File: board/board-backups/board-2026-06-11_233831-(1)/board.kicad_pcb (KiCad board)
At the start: 2 copper layers, 42.6 x 75.4 mm, 27 parts, among them J1 port attiny, J10 BMS Bat +, J11 BMS Bat gnd, J12 BMS out -, J13 BMS in +5v, J14 BMS in gnd, J15 alim mp3 -, J17 next, J18 vol -, J2 Conn_01x02_Pin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

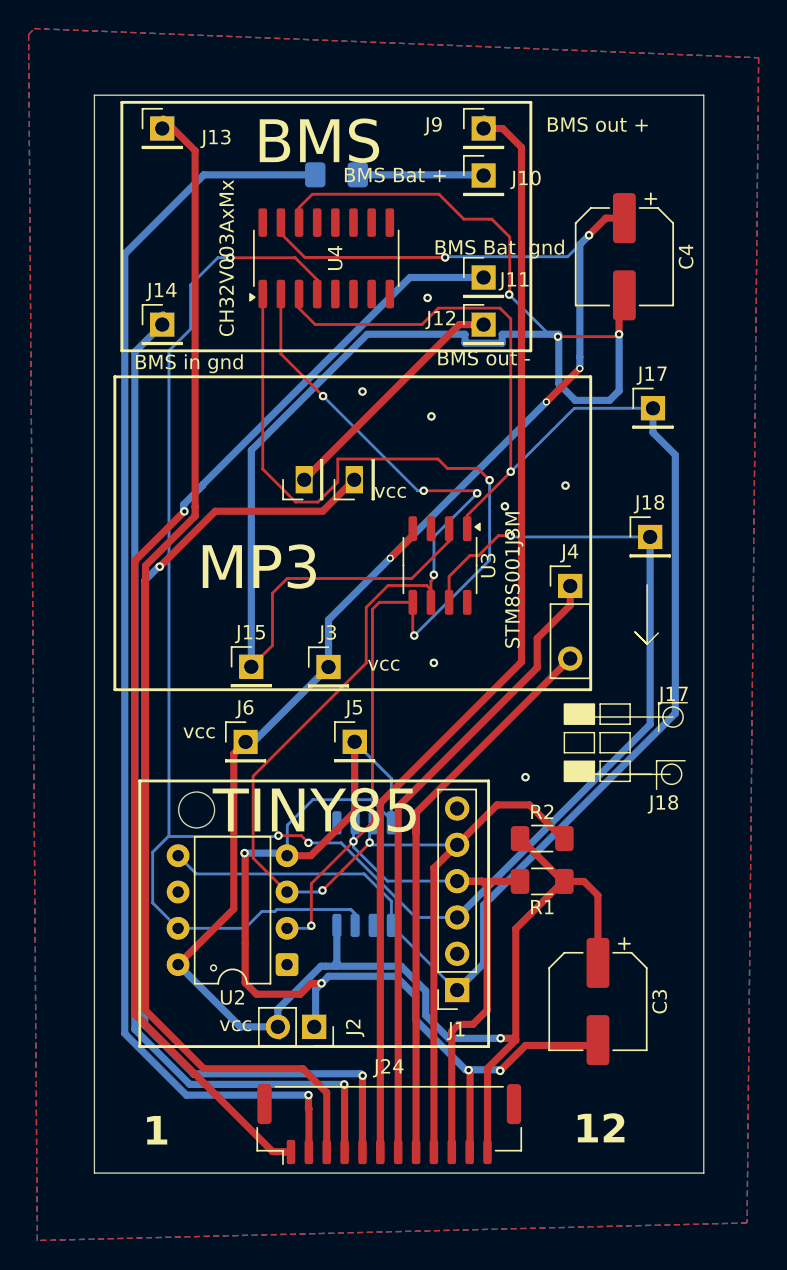
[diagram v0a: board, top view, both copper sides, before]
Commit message: correction inversion polarité sur l'alimentation
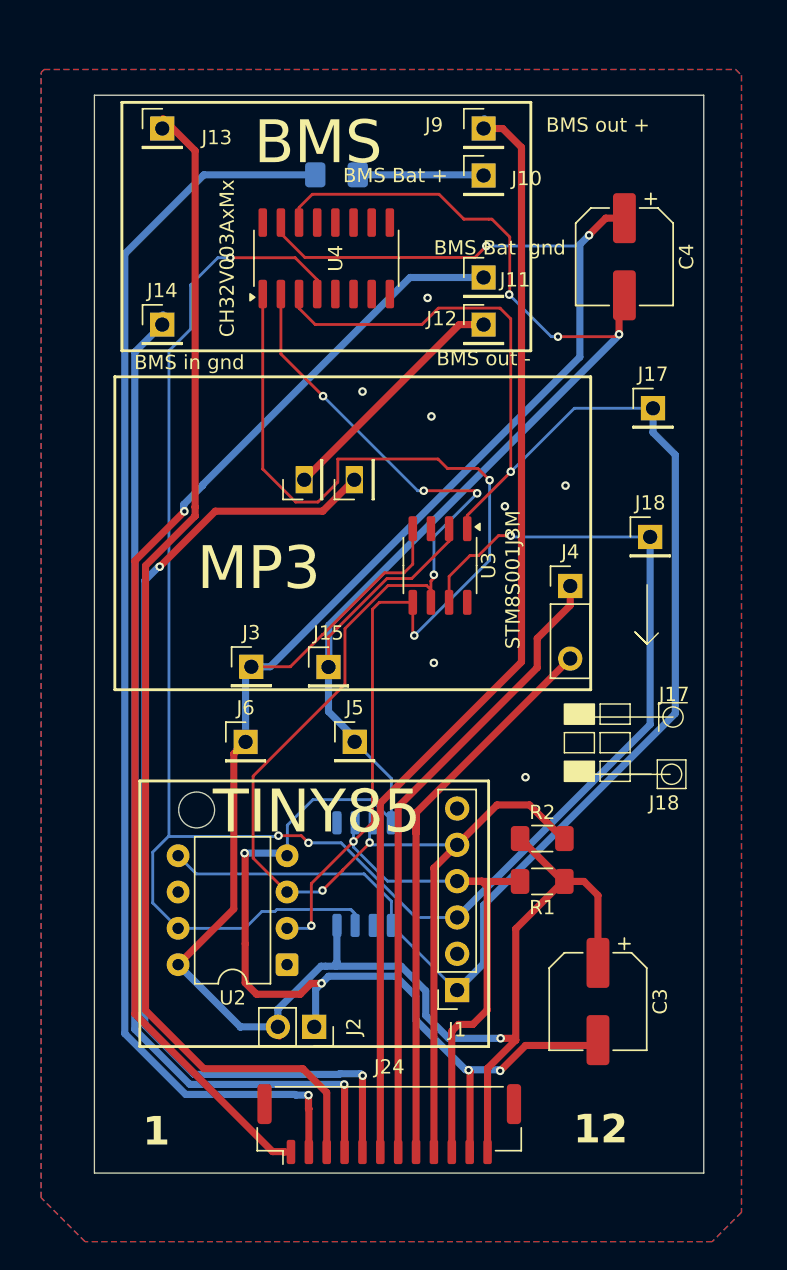
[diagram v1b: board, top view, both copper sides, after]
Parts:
- moved J15 5.40 mm to (79.9, 79.0)
- moved J3 5.40 mm to (74.5, 79.0)
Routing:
- net GND: track 187.9 -> 154.2 mm, vias 15 -> 14
- net VCC: track 160.9 -> 175.5 mm, vias 6 -> 3
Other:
- board text removed: "vcc"
